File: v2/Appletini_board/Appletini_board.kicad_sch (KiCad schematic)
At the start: 14 parts, among them J1 Conn_02x25_Counter_Clockwise, Q1 TP0610T, U2 Pico, U3 Teensy4.1

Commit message: v2 board first draft done
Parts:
- removed R3: 10K, Resistor_SMD:R_0402_1005Metric, symbol Device:R_US
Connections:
- net PICO_~{DMA_CYCLE} is gone; now on net PICO_DMA_CYCLE: U2.25 (GPIO19)
- net +5V: now also Q1.3 (D)
- net PICO_CTRL_~{DMA}: now also U3.6 (GPIO9.6)
- net PICO_CTRL_~{INH}: now also U3.5 (GPIO9.5)
- net PICO_CTRL_~{RDY}: now also U3.7 (GPIO9.8)
- net PICO_DMA_CYCLE: now also U3.9 (GPIO7.17); no longer U3.6 (GPIO9.6)
- net PICO_D_~{LEBA}: now also U2.22 (GPIO17); no longer U2.21 (GPIO16)
- net PICO_D_~{OEAB}: now also U2.21 (GPIO16); no longer U2.22 (GPIO17)
- net TEENSY_CTRL_~{IRQ}: now also U3.4 (GPIO9.4); no longer U3.7 (GPIO9.8)
- net TEENSY_REQ_DMA: now also U3.27 (GPIO7.28); no longer U3.26 (GPIO7.29)
- net TEENSY_REQ_~{DMAOUT}: now also U3.26 (GPIO7.29); no longer U3.27 (GPIO7.28)
- net VIN: no longer Q1.3 (D)
- net ~{DMA}: no longer U3.4 (GPIO9.4)
- net ~{IRQ}: no longer U3.5 (GPIO9.5)
- net LEVEL_ENABLE: no longer names the net of U2.32 (GPIO27_ADC1)
- no-connect marks 62 -> 63
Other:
- sheet Bus transceivers ports: added none; removed LEVEL_ENABLE

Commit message: fixes
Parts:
- removed R10: 10K, Resistor_SMD:R_0402_1005Metric, symbol Device:R_US
- renumbered C3 to C1, C4 to C2, C5 to C3, C6 to C4, R11 to R1, R1 to R3, R2 to R4, U2 to U1, U3 to U2
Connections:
- net TEENSY_CTRL_~{IRQ} is gone; now on net TEENSY_REQ_DMA: U2.4 (GPIO9.4)
- net GND: now also U1.13 (GND), U1.18 (GND), U1.23 (GND), U1.28 (GND), U1.3 (GND), U1.33 (AGND), U1.38 (GND), U1.8 (GND)
- net TEENSY_REQ_DMA: no longer U2.27 (GPIO7.28)
- net ~{DMA}: now also U1.29 (GPIO22), U2.6 (GPIO9.6)
- net PICO_CTRL_~{DMA}: no longer names the net of U1.6 (GPIO4)
- net PICO_CTRL_~{DMA}: no longer U2.6 (GPIO9.6)
- net PICO_CTRL_~{INH}: no longer names the net of U1.7 (GPIO5)
- net PICO_CTRL_~{INH}: no longer U2.5 (GPIO9.5)
- net PICO_CTRL_~{RDY}: no longer names the net of U1.9 (GPIO6)
- net PICO_CTRL_~{RDY}: no longer U2.7 (GPIO9.8)
- net PICO_DMA_CYCLE renamed DMA_CYCLE_ACTIVE
- net PICO_TEENSY_~{IRQ} renamed TEENSY_~{IRQ}
- net TEENSY_~{INH}: no longer names the net of U2.8 (GPIO7.10)
- net TEENSY_~{INH}: no longer U1.17 (GPIO13)
- new net TEENSY_REQ_~{IRQ}: U2.27 (GPIO7.28)
- new net ~{INH}: U2.5 (GPIO9.5)
- new net ~{RDY}: U2.7 (GPIO9.8)
- no-connect marks 63 -> 59
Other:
- sheet Bus transceivers ports: added DMA_CYCLE_ACTIVE, TEENSY_REQ_~{IRQ}, ~{INH}, ~{RDY}; removed PICO_CTRL_~{DMA}, PICO_CTRL_~{INH}, PICO_CTRL_~{RDY}, PICO_DMA_CYCLE, TEENSY_CTRL_~{IRQ}, ~{DMAIN}, ~{INTIN}, ~{IRQ}
- moved on the sheet: R1

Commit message: pcb debugging, first draft of PIO
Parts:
- added J2, J3: Conn_01x20, Connector_PinSocket_2.54mm:PinSocket_1x20_P2.54mm_Vertical, symbol Connector_Generic:Conn_01x20
- added J4, J5: Conn_01x24, Connector_PinSocket_2.54mm:PinSocket_1x24_P2.54mm_Vertical, symbol Connector_Generic:Conn_01x24
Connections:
- net +3.3V: now also J4.22 (Pin_22); no longer U2.46 (3V3)
- net B0: now also J4.17 (Pin_17); no longer U2.41 (GPIO6.16)
- net B1: now also J4.16 (Pin_16); no longer U2.40 (GPIO6.17)
- net B10: now also J4.18 (Pin_18); no longer U2.42 (GPIO6.26)
- net B11: now also J4.19 (Pin_19); no longer U2.43 (GPIO6.27)
- net B12: now also J4.6 (Pin_6); no longer U2.30 (GPIO6.28)
- net B13: now also J4.7 (Pin_7); no longer U2.31 (GPIO6.29)
- net B14: now also J5.18 (Pin_18); no longer U2.18 (GPIO6.30)
- net B15: now also J5.19 (Pin_19); no longer U2.19 (GPIO6.31)
- net B2: now also J4.12 (Pin_12); no longer U2.36 (GPIO6.18)
- net B3: now also J4.13 (Pin_13); no longer U2.37 (GPIO6.19)
- net B4: now also J4.8 (Pin_8); no longer U2.32 (GPIO6.20)
- net B5: now also J4.9 (Pin_9); no longer U2.33 (GPIO6.21)
- net B6: now also J4.15 (Pin_15); no longer U2.39 (GPIO6.22)
- net B7: now also J4.14 (Pin_14); no longer U2.38 (GPIO6.23)
- net B8: now also J4.20 (Pin_20); no longer U2.44 (GPIO6.24)
- net B9: now also J4.21 (Pin_21); no longer U2.45 (GPIO6.25)
- net BUS_~{ENABLE}: now also J3.14 (Pin_14); no longer U1.34 (GPIO28_ADC2)
- net DMA_CYCLE_ACTIVE: now also J3.1 (Pin_1), J5.9 (Pin_9); no longer U1.25 (GPIO19), U2.9 (GPIO7.17)
- net GND: now also J2.13 (Pin_13), J2.18 (Pin_18), J2.3 (Pin_3), J2.8 (Pin_8), J3.13 (Pin_13), J3.18 (Pin_18), J3.3 (Pin_3), J3.8 (Pin_8), J4.10 (Pin_10), J4.23 (Pin_23), J5.1 (Pin_1); no longer U1.13 (GND), U1.18 (GND), U1.23 (GND), U1.28 (GND), U1.3 (GND), U1.33 (AGND), U1.38 (GND), U1.8 (GND), U2.1 (GND), U2.34 (GND), U2.47 (GND)
- net M2B0: now also J5.2 (Pin_2); no longer U2.2 (GPIO6.3)
- net M2SEL: now also J5.3 (Pin_3); no longer U2.3 (GPIO6.2)
- net PHI0: now also J3.11 (Pin_11), J5.16 (Pin_16); no longer U1.31 (GPIO26_ADC0), U2.16 (GPIO6.12)
- net PICO_A_~{LEBA}: now also J3.7 (Pin_7); no longer U1.26 (GPIO20)
- net PICO_A_~{OEAB}: now also J3.5 (Pin_5); no longer U1.27 (GPIO21)
- net PICO_D_~{LEBA}: now also J3.6 (Pin_6); no longer U1.22 (GPIO17)
- net PICO_D_~{OEAB}: now also J3.2 (Pin_2); no longer U1.21 (GPIO16)
- net R~{W}: now also J5.17 (Pin_17); no longer U2.17 (GPIO6.13)
- net TEENSY_A_~{LEAB}: now also J5.14 (Pin_14); no longer U2.14 (GPIO7.1)
- net TEENSY_A_~{OEBA}: now also J5.13 (Pin_13); no longer U2.13 (GPIO7.2)
- net TEENSY_D_~{LEAB}: now also J5.10 (Pin_10); no longer U2.10 (GPIO7.16)
- net TEENSY_D_~{OEBA}: now also J4.4 (Pin_4); no longer U2.28 (GPIO7.18)
- net TEENSY_READY: now also J2.1 (Pin_1), J5.24 (Pin_24); no longer U1.19 (GPIO14), U2.24 (GPIO7.12)
- net TEENSY_REQ_DMA: now also J5.4 (Pin_4); no longer U2.4 (GPIO9.4)
- net TEENSY_REQ_~{DMAOUT}: now also J4.2 (Pin_2); no longer U2.26 (GPIO7.29)
- net TEENSY_REQ_~{IRQ}: now also J4.3 (Pin_3); no longer U2.27 (GPIO7.28)
- net TEENSY_~{EMIT_DATA}: now also J3.10 (Pin_10), J4.5 (Pin_5); no longer U1.16 (GPIO12), U2.29 (GPIO7.19)
- net TEENSY_~{IRQ}: now also J3.9 (Pin_9), J5.21 (Pin_21); no longer U1.24 (GPIO18), U2.21 (GPIO9.31)
- net VIN: now also J4.24 (Pin_24); no longer U2.48 (VIN)
- net ~{DMA}: now also J3.4 (Pin_4), J5.6 (Pin_6); no longer U1.29 (GPIO22), U2.6 (GPIO9.6)
- net ~{INH}: now also J5.5 (Pin_5); no longer U2.5 (GPIO9.5)
- net ~{RDY}: now also J5.7 (Pin_7); no longer U2.7 (GPIO9.8)
- net at Q1.2 (S): now also J3.19 (Pin_19); no longer U1.39 (VSYS)
- net at Q1.1 (G): now also J3.20 (Pin_20); no longer U1.40 (VBUS)
- no-connect marks 59 -> 37
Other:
- moved on the sheet: JP1, Q1, R4

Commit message: checkpoint before lvc573 rework
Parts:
- C1, C2, C3, C4: value 100pF -> 100nF; LCSC (none) -> C24497
- J2, J3: LCSC (none) -> C50984
- J4, J5: LCSC (none) -> C2883741
- JP1: LCSC (none) -> C5360898
- Q1: LCSC (none) -> C5261054
- R1, R3, R4: LCSC (none) -> C2991755
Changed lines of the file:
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@@
+      (effects (font (size 1.27 1.27)) hide)
+    )
+    (property "LCSC" "C2883741" (at 149.86 132.08 0)
+      (effects (font (size 1.27 1.27)) hide)
+    )
+    (property "Field5" "" (at 149.86 132.08 0)
       (effects (font (size 1.27 1.27)) hide)
     )
@@
       (effects (font (size 1.27 1.27)) hide)
     )
+    (property "LCSC" "C2991755" (at 135.89 40.64 0)
+      (effects (font (size 1.27 1.27)) hide)
+    )
     (pin "1")
     (pin "2")
@@
     )
     (property "Datasheet" "~" (at 138.43 129.54 0)
+      (effects (font (size 1.27 1.27)) hide)
+    )
+    (property "LCSC" "C2883741" (at 138.43 129.54 0)
+      (effects (font (size 1.27 1.27)) hide)
+    )
+    (property "Field5" "" (at 138.43 129.54 0)
       (effects (font (size 1.27 1.27)) hide)
     )
@@
       (effects (font (size 1.27 1.27)) (justify left))
     )
-    (property "Value" "100pF" (at 212.09 137.795 0)
+    (property "Value" "100nF" (at 212.09 137.795 0)
       (effects (font (size 1.27 1.27)) (justify left))
     )
@@
     )
     (property "Datasheet" "~" (at 208.28 135.89 0)
+      (effects (font (size 1.27 1.27)) hide)
+    )
+    (property "LCSC" "C24497" (at 208.28 135.89 0)
+      (effects (font (size 1.27 1.27)) hide)
+    )
+    (property "Field5" "" (at 208.28 135.89 0)
       (effects (font (size 1.27 1.27)) hide)
     )
@@
       (effects (font (size 1.27 1.27)) (justify left))
     )
-    (property "Value" "100pF" (at 241.3 137.795 0)
+    (property "Value" "100nF" (at 241.3 137.795 0)
       (effects (font (size 1.27 1.27)) (justify left))
     )
@@
       (effects (font (size 1.27 1.27)) hide)
     )
+    (property "LCSC" "C24497" (at 237.49 135.89 0)
+      (effects (font (size 1.27 1.27)) hide)
+    )
     (pin "1")
     (pin "2")
@@
       (effects (font (size 1.27 1.27)) hide)
     )
+    (property "LCSC" "C2991755" (at 93.98 33.02 0)
+      (effects (font (size 1.27 1.27)) hide)
+    )
     (pin "1")
     (pin "2")
@@
       (effects (font (size 1.27 1.27)) (justify left))
     )
-    (property "Value" "100pF" (at 227.33 137.795 0)
+    (property "Value" "100nF" (at 227.33 137.795 0)
       (effects (font (size 1.27 1.27)) (justify left))
     )
@@
     )
     (property "Datasheet" "~" (at 223.52 135.89 0)
+      (effects (font (size 1.27 1.27)) hide)
+    )
+    (property "LCSC" "C24497" (at 223.52 135.89 0)
       (effects (font (size 1.27 1.27)) hide)
     )
@@
       (effects (font (size 1.27 1.27)) (justify left) hide)
     )
+    (property "LCSC" "C5261054" (at 135.89 26.67 0)
+      (effects (font (size 1.27 1.27)) hide)
+    )
     (pin "1")
     (pin "2")
@@
       (effects (font (size 1.27 1.27)) (justify left))
     )
-    (property "Value" "100pF" (at 256.54 137.795 0)
+    (property "Value" "100nF" (at 256.54 137.795 0)
       (effects (font (size 1.27 1.27)) (justify left))
     )
@@
     )
     (property "Datasheet" "~" (at 252.73 135.89 0)
+      (effects (font (size 1.27 1.27)) hide)
+    )
+    (property "LCSC" "C24497" (at 252.73 135.89 0)
       (effects (font (size 1.27 1.27)) hide)
     )
@@
     )
     (property "Datasheet" "~" (at 116.84 52.07 0)
+      (effects (font (size 1.27 1.27)) hide)
+    )
+    (property "LCSC" "C50984" (at 116.84 52.07 0)
       (effects (font (size 1.27 1.27)) hide)
     )
@@
       (effects (font (size 1.27 1.27)) hide)
     )
+    (property "LCSC" "C5360898" (at 168.91 101.6 0)
+      (effects (font (size 1.27 1.27)) hide)
+    )
     (pin "1")
     (pin "2")
@@
     )
     (property "Datasheet" "~" (at 148.59 54.61 0)
+      (effects (font (size 1.27 1.27)) hide)
+    )
+    (property "LCSC" "C2991755" (at 148.59 54.61 0)
       (effects (font (size 1.27 1.27)) hide)
     )
@@
       (effects (font (size 1.27 1.27)) hide)
     )
+    (property "LCSC" "C50984" (at 125.73 54.61 0)
+      (effects (font (size 1.27 1.27)) hide)
+    )

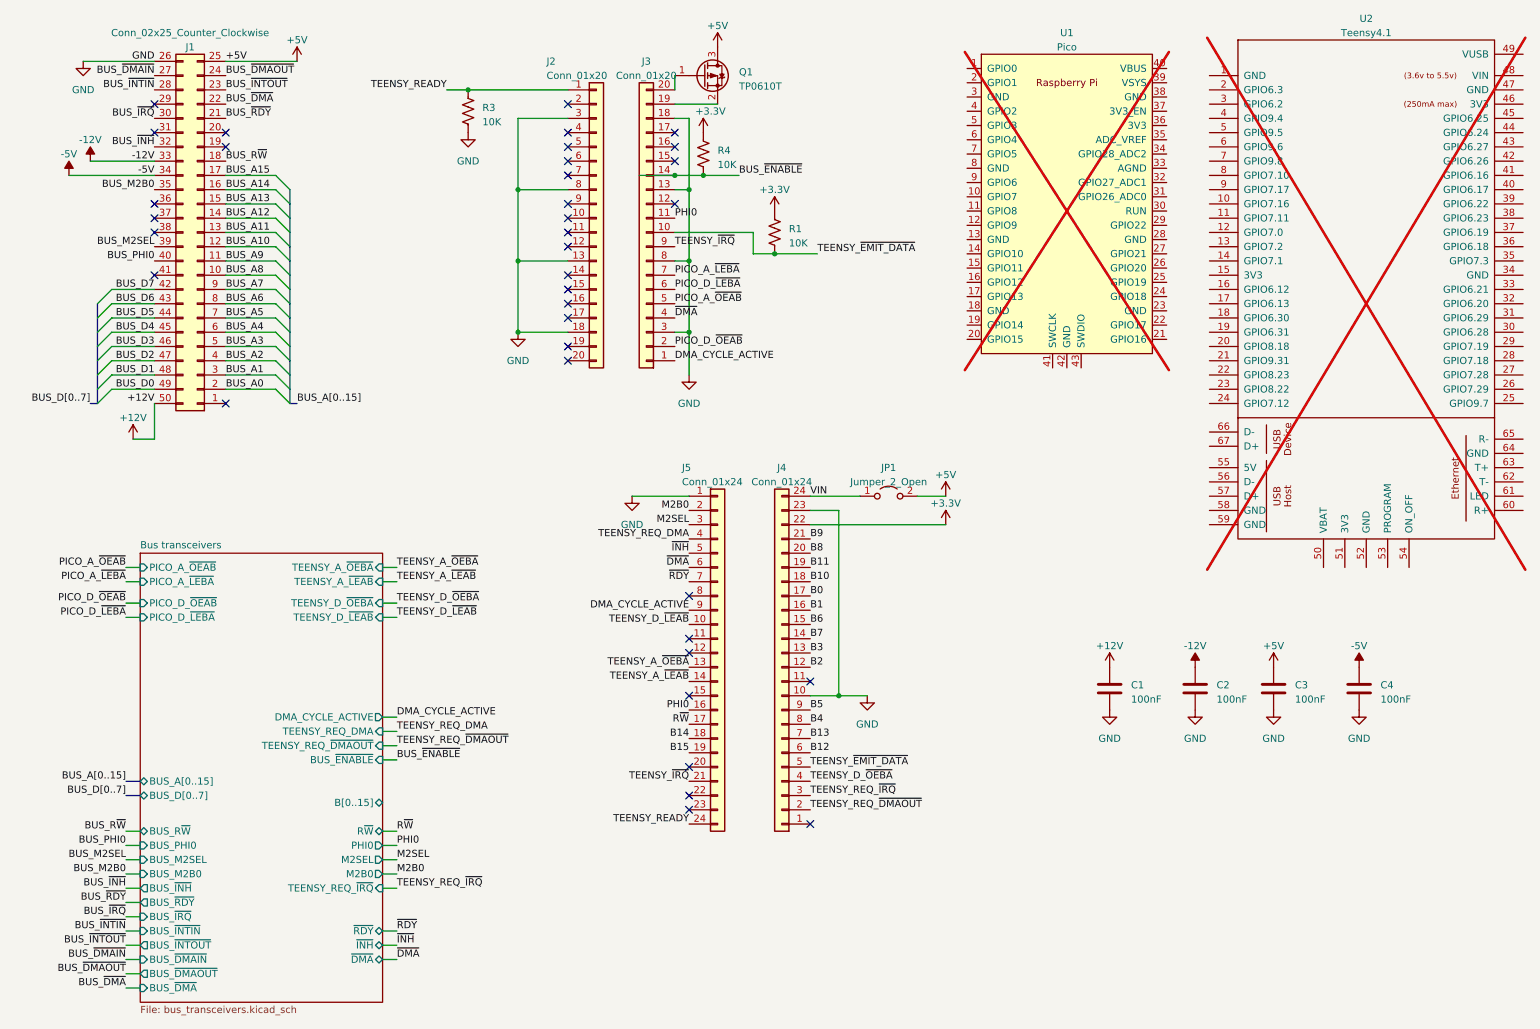
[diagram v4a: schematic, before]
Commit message: board ordered
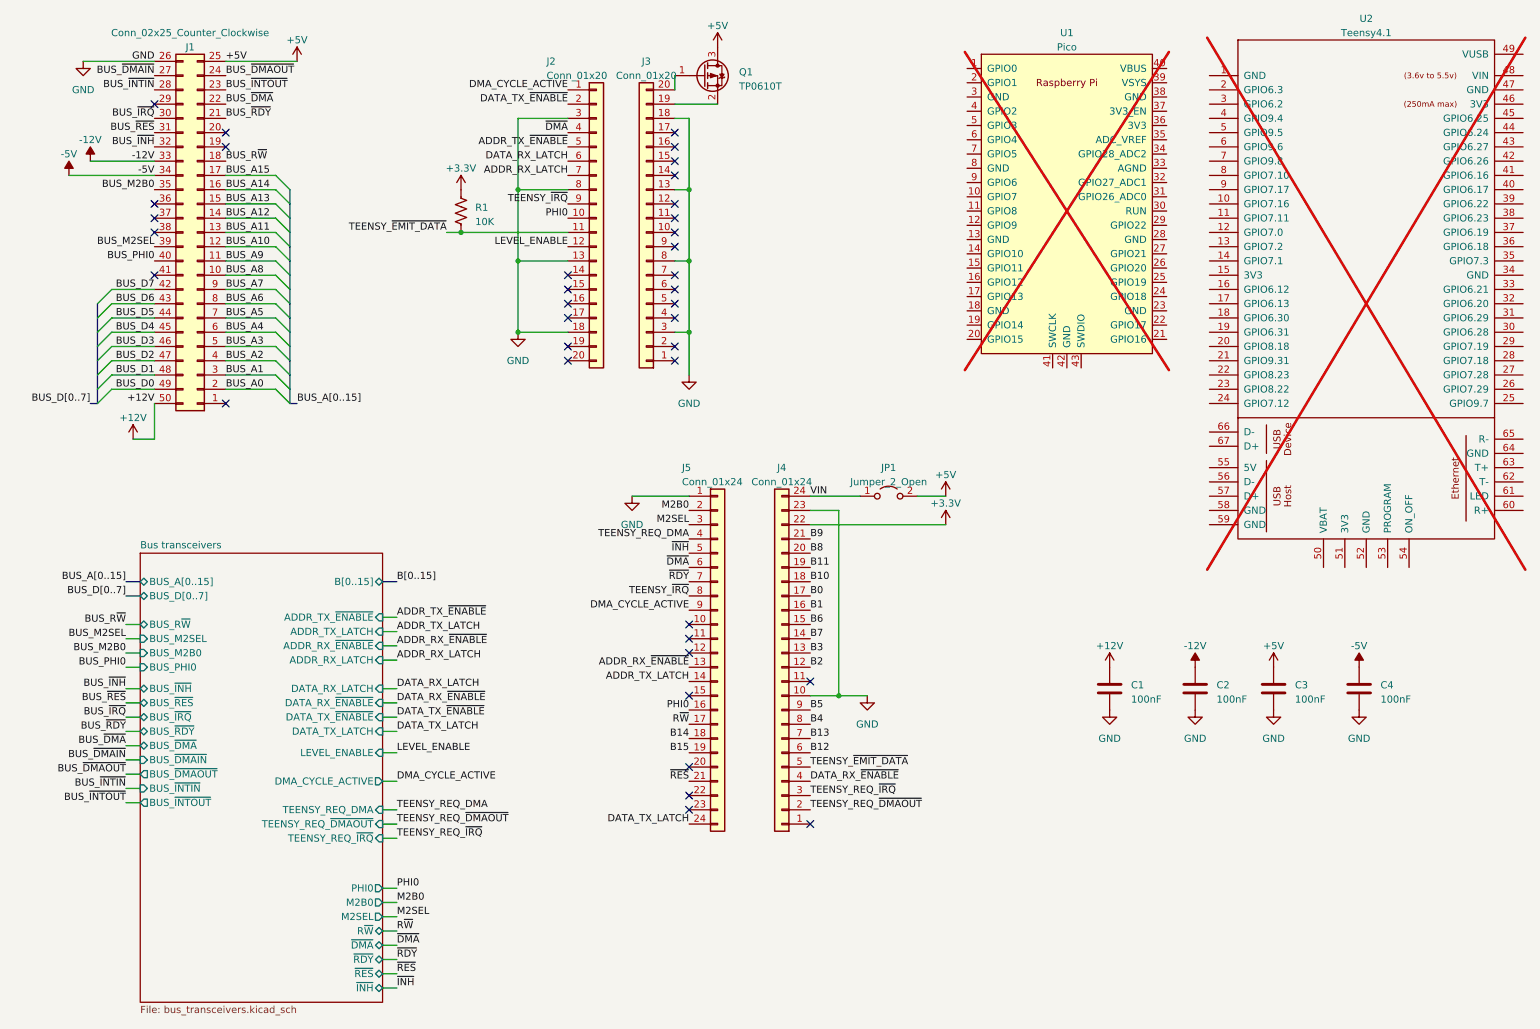
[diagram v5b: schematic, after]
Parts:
- removed R3, R4: 10K, Resistor_SMD:R_0402_1005Metric, symbol Device:R_US
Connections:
- net DMA_CYCLE_ACTIVE: now also J2.1 (Pin_1); no longer J3.1 (Pin_1)
- net PHI0: now also J2.10 (Pin_10); no longer J3.11 (Pin_11)
- net TEENSY_~{EMIT_DATA}: now also J2.11 (Pin_11); no longer J3.10 (Pin_10)
- net TEENSY_~{IRQ}: now also J2.9 (Pin_9), J5.8 (Pin_8); no longer J3.9 (Pin_9), J5.21 (Pin_21)
- net ~{DMA}: now also J2.4 (Pin_4); no longer J3.4 (Pin_4)
- net LEVEL_ENABLE: now reaches J2.12 (Pin_12)
- net DATA_TX_~{ENABLE}: now reaches J2.2 (Pin_2)
- net ADDR_TX_~{ENABLE}: now reaches J2.5 (Pin_5)
- net DATA_RX_LATCH: now reaches J2.6 (Pin_6)
- net ADDR_RX_LATCH: now reaches J2.7 (Pin_7)
- net BUS_~{RES}: now reaches J1.31 (Pin_31)
- net BUS_~{ENABLE}: no longer names the net of J3.14 (Pin_14)
- net PICO_A_~{LEBA}: no longer names the net of J3.7 (Pin_7)
- net PICO_A_~{OEAB}: no longer names the net of J3.5 (Pin_5)
- net PICO_D_~{LEBA}: no longer names the net of J3.6 (Pin_6)
- net PICO_D_~{OEAB}: no longer names the net of J3.2 (Pin_2)
- net TEENSY_A_~{LEAB} renamed ADDR_TX_LATCH
- net TEENSY_A_~{OEBA} renamed ADDR_RX_~{ENABLE}
- net TEENSY_D_~{LEAB}: no longer names the net of J5.10 (Pin_10)
- net TEENSY_D_~{OEBA} renamed DATA_RX_~{ENABLE}
- net TEENSY_READY renamed DATA_TX_LATCH
- net DATA_TX_LATCH: no longer J2.1 (Pin_1)
- new net ~{RES}: J5.21 (Pin_21)
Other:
- sheet Bus transceivers ports: added ADDR_RX_LATCH, ADDR_RX_~{ENABLE}, ADDR_TX_LATCH, ADDR_TX_~{ENABLE}, BUS_~{RES}, DATA_RX_LATCH, DATA_RX_~{ENABLE}, DATA_TX_LATCH, DATA_TX_~{ENABLE}, LEVEL_ENABLE, ~{RES}; removed BUS_~{ENABLE}, PICO_A_~{LEBA}, PICO_A_~{OEAB}, PICO_D_~{LEBA}, PICO_D_~{OEAB}, TEENSY_A_~{LEAB}, TEENSY_A_~{OEBA}, TEENSY_D_~{LEAB}, TEENSY_D_~{OEBA}
